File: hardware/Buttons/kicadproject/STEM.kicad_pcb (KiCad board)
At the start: 2 copper layers, 70 x 60.6 mm, 26 parts, among them IC1 PIC16F18446-I_SS, J1 PICKit3, J2 MASTER

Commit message: Update Sensor Module
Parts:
- removed the G*** at (112.9, 90.8)
- removed the G*** at (131.1, 89.4)
- removed REF**: PinHeader_1x06_P2.54mm_Vertical_SMD, Logo:PinHeader_1x06_P2.54mm_Vertical_SMD
- removed S1, S2, S3, S4: 3006.2114, TactileSwitchLed_30062114_footprint:30062114
- added ?: , graphics:dramco, F.Cu at (113.5, 89.4)
- added G***: LOGO, graphics:kuleuven, F.Cu at (130.6, 89.4)
- added U1: button, Button_Ali:aliButton, F.Cu at (140.0, 115.2)
- added U3: button, Button_Ali:aliButton, F.Cu at (105.0, 115.2)
- added U4: button, Button_Ali:aliButton, F.Cu at (122.5, 102.3)
- added Ue: button, Button_Ali:aliButton, F.Cu at (122.5, 128.3)
- C1, C2, C3, C4, C5: footprint Capacitor_SMD:C_0805_2012Metric_Pad1.15x1.40mm_HandSolder -> Capacitor_SMD:C_0805_2012Metric_Pad1.18x1.45mm_HandSolder
- R1, R10, R2, R3, R4, R9: footprint Resistor_SMD:R_0805_2012Metric_Pad1.15x1.40mm_HandSolder -> Resistor_SMD:R_0805_2012Metric_Pad1.20x1.40mm_HandSolder
- R5, R7: value 1k -> 100k; footprint Resistor_SMD:R_0805_2012Metric_Pad1.15x1.40mm_HandSolder -> Resistor_SMD:R_0805_2012Metric_Pad1.20x1.40mm_HandSolder
- R6, R8: value 100k -> 1k; footprint Resistor_SMD:R_0805_2012Metric_Pad1.15x1.40mm_HandSolder -> Resistor_SMD:R_0805_2012Metric_Pad1.20x1.40mm_HandSolder
- moved R7 32.8 mm to (132.7, 101.6), turned to 180 degrees
- moved R2 30.4 mm to (144.1, 102.9), turned to 0 degrees
- moved R9 27.8 mm to (132.7, 97.8)
- moved R5 25.8 mm to (110.5, 106.0)
- moved C5 24.9 mm to (132.7, 99.7), turned to 180 degrees
- moved C4 24.5 mm to (110.5, 104.1), turned to 0 degrees
- moved R3 22.0 mm to (144.1, 104.7)
- moved C2 13.0 mm to (144.1, 101.0), turned to 0 degrees
- moved R8 9.94 mm to (110.5, 102.2)
- moved C3 9.62 mm to (132.7, 126.4)
- moved R4 9.38 mm to (132.7, 128.3)
- moved C1 6.76 mm to (115.6, 109.9), turned to 180 degrees
- moved R1 2.23 mm to (115.6, 111.8), turned to 180 degrees
- moved R6 1.75 mm to (132.7, 124.5)
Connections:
- net /RA5 renamed Net-(IC1-Pad2)
- R5 pad 1: /LSW2 -> +3V3
- R5 pad 2: Net-(R5-Pad2) -> /SW3
- R6 pad 1: +3V3 -> /LSW2
- R6 pad 2: /SW3 -> Net-(R6-Pad2)
- R7 pad 1: /LSW3 -> +3V3
- R7 pad 2: Net-(R7-Pad2) -> /SW4
- R8 pad 1: +3V3 -> /LSW3
- R8 pad 2: /SW4 -> Net-(R8-Pad2)
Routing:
- net +3V3: track 184.1 -> 149.2 mm, vias 0 -> 3
- net /LSW4: track 3.74 -> 37.1 mm, vias 0 -> 2
- net GND: track 43.6 -> 13.4 mm
- net /INT: track 55.4 -> 36.3 mm
- net /LSW1: track 16.1 -> 32.5 mm
- net /RC1: track 42.0 -> 30.6 mm, vias 2 -> 0
- net /LSW2: track 16.0 -> 27.1 mm, vias 0 -> 2
- net Net-(R6-Pad2): track 0.00 -> 10.9 mm, vias 0 -> 2
- net Net-(R9-Pad2): track 20.4 -> 10.3 mm
- net Net-(R8-Pad2): track 0.00 -> 9.83 mm
- net Net-(R7-Pad2): track 9.80 -> 0.00 mm
- net /SCL: track 33.8 -> 24.3 mm
- net /SW1: track 55.6 -> 47.4 mm, vias 2 -> 3
- net /LSW3: track 17.1 -> 24.7 mm, vias 0 -> 2
- net Net-(R5-Pad2): track 7.22 -> 0.00 mm
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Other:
- board text added: "IWAST Buttons V4"

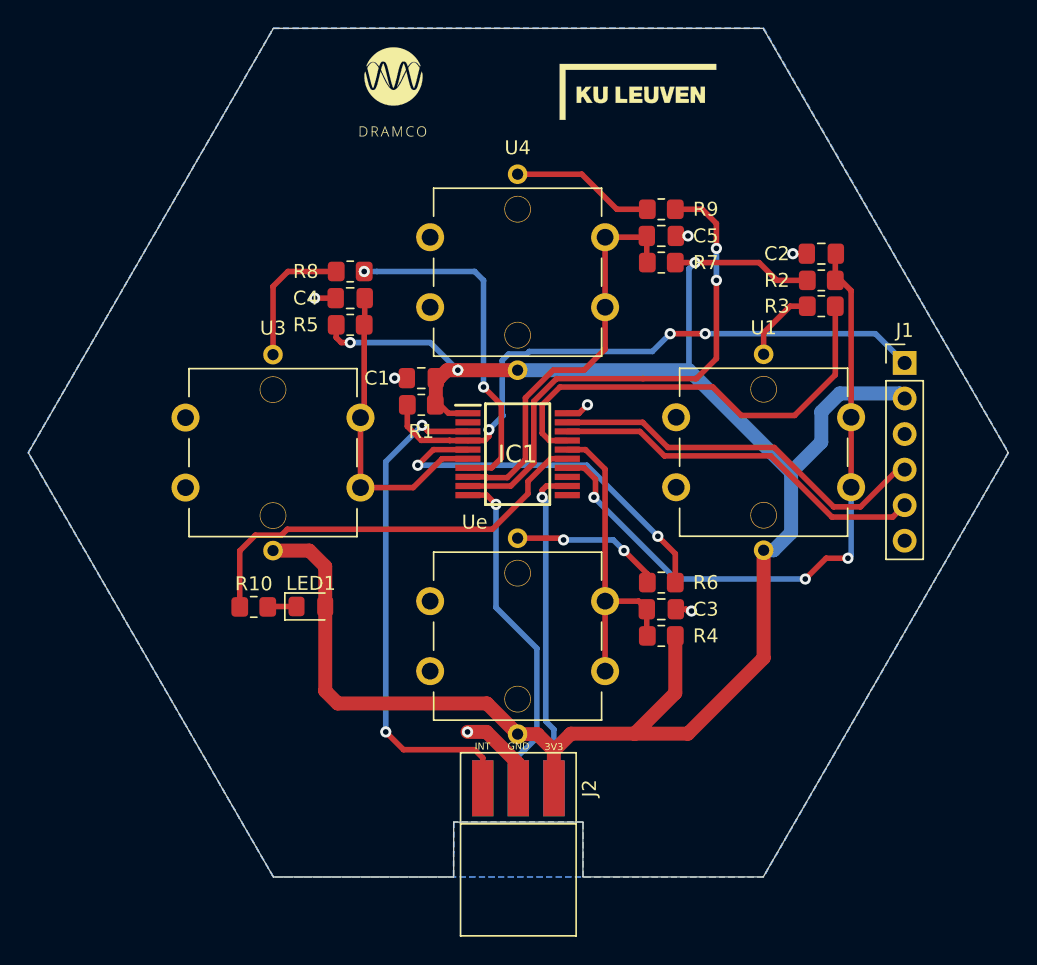
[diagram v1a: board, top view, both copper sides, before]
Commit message: Update Footprint Button
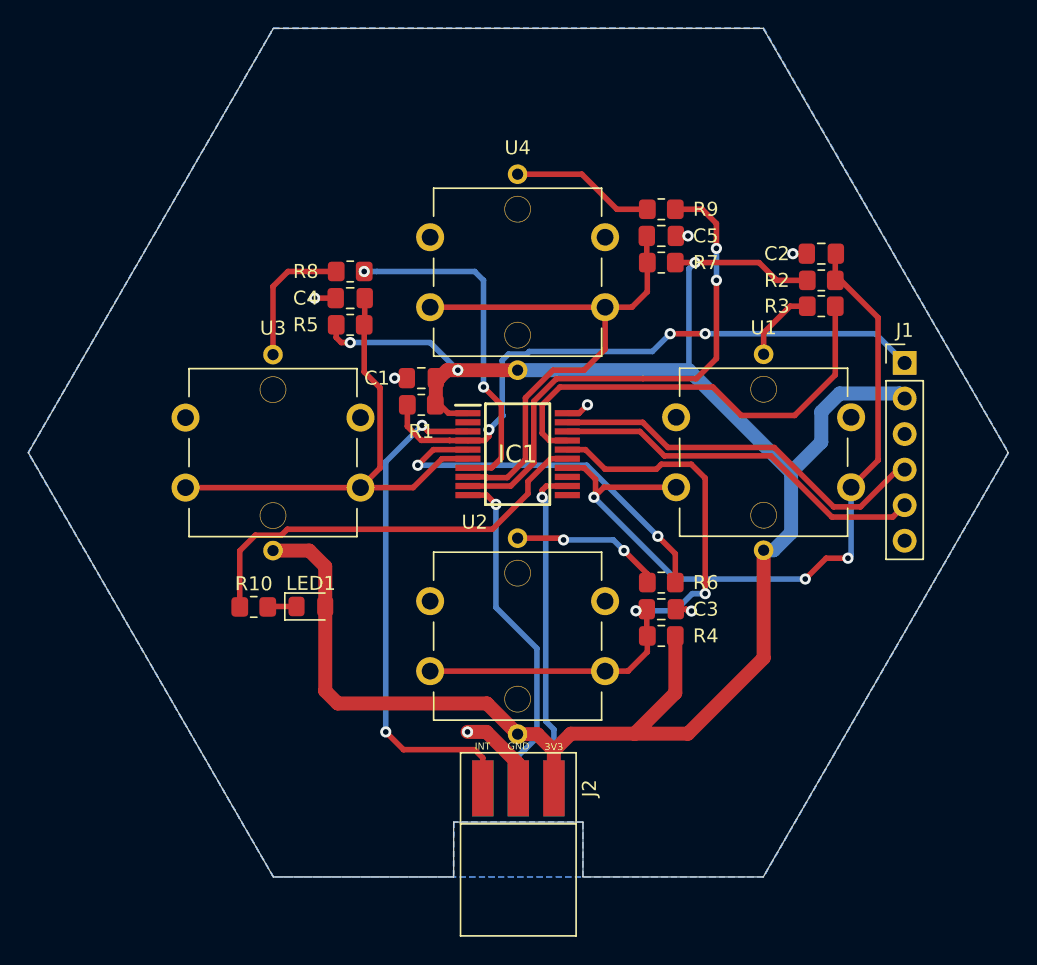
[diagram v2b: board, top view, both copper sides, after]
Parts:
- removed ?: , graphics:dramco
- removed G***: LOGO, graphics:kuleuven
- renumbered Ue to U2
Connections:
- IC1 pad 11: /RB6 -> (no net)
- IC1 pad 13: /RB4 -> (no net)
- IC1 pad 2: Net-(IC1-Pad2) -> (no net)
- J1 pad 6: Net-(J1-Pad6) -> (no net)
- J2 pad 6: /VBAT -> (no net)
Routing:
- net /SW2: track 22.8 -> 44.7 mm, vias 0 -> 2
- net /SW3: track 22.2 -> 35.6 mm
- net /SW4: track 29.1 -> 39.3 mm
- net /SW1: track 47.4 -> 55.2 mm
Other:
- board text added: "IWAST Buttons V5"
- board text removed: "IWAST Buttons V4"

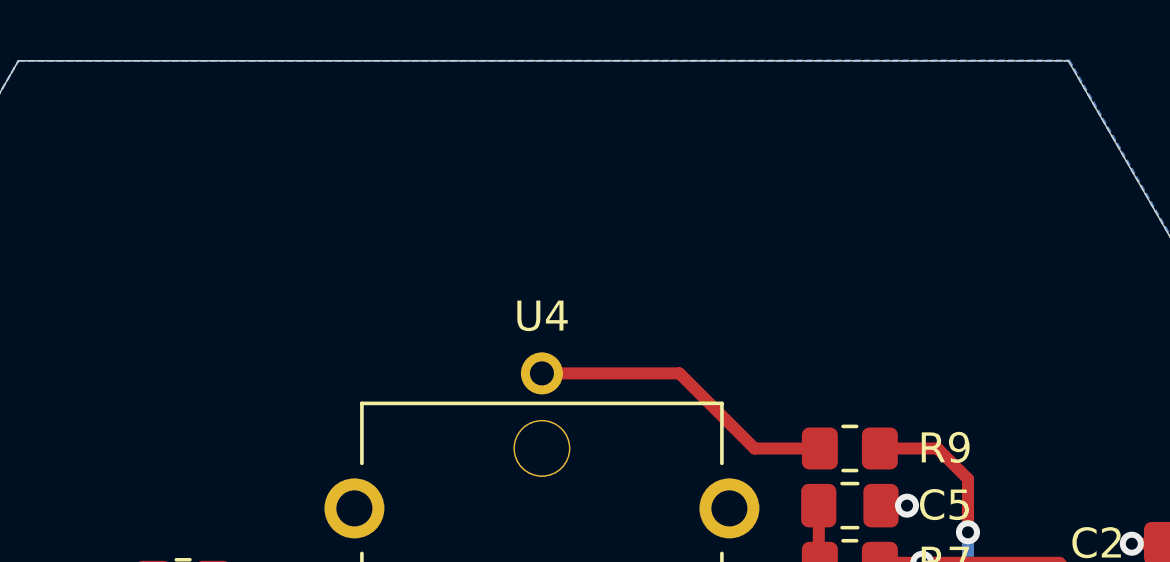
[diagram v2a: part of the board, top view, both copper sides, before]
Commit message: Buttons gerber update with logos
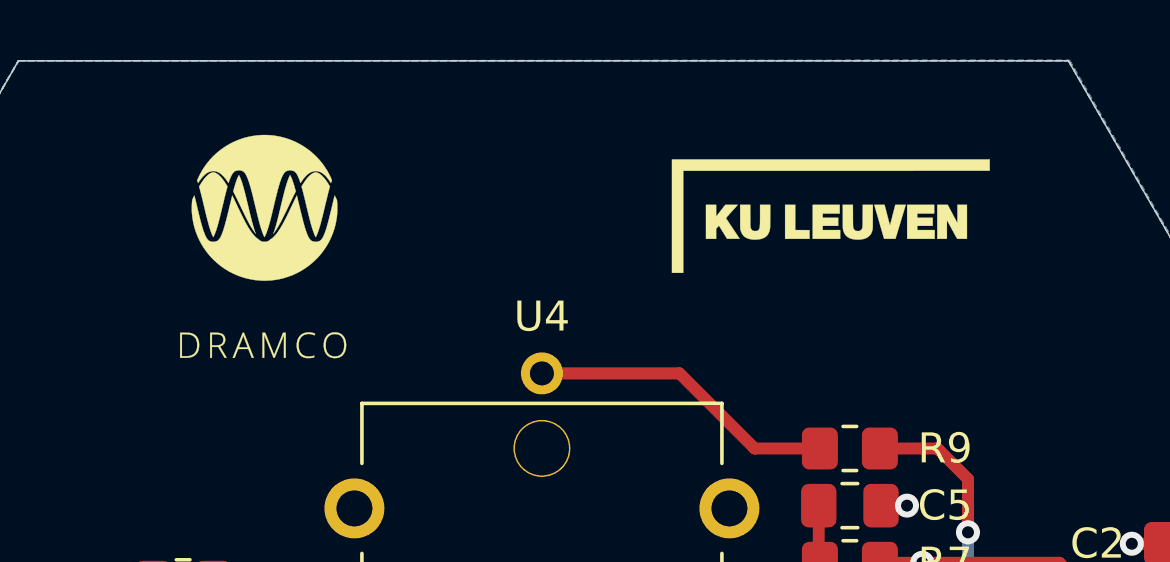
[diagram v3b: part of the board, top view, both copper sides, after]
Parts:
- added G***: LOGO, logos:dramco_logo, F.Cu at (113.2, 91.1)
- added G***: LOGO, logos:kul_logo, F.Cu at (132.1, 90.0)
